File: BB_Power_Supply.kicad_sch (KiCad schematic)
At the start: 17 parts, among them J1 Barrel_Jack_Switch, J2 Conn_01x03_Male, J3 Conn_01x02_Male, J4 Screw_Terminal_01x02, J5 Conn_01x03_Male, J6 Conn_01x02_Male, J7 Screw_Terminal_01x02, U1 LM317_TO-220, U2 LM7805_TO220

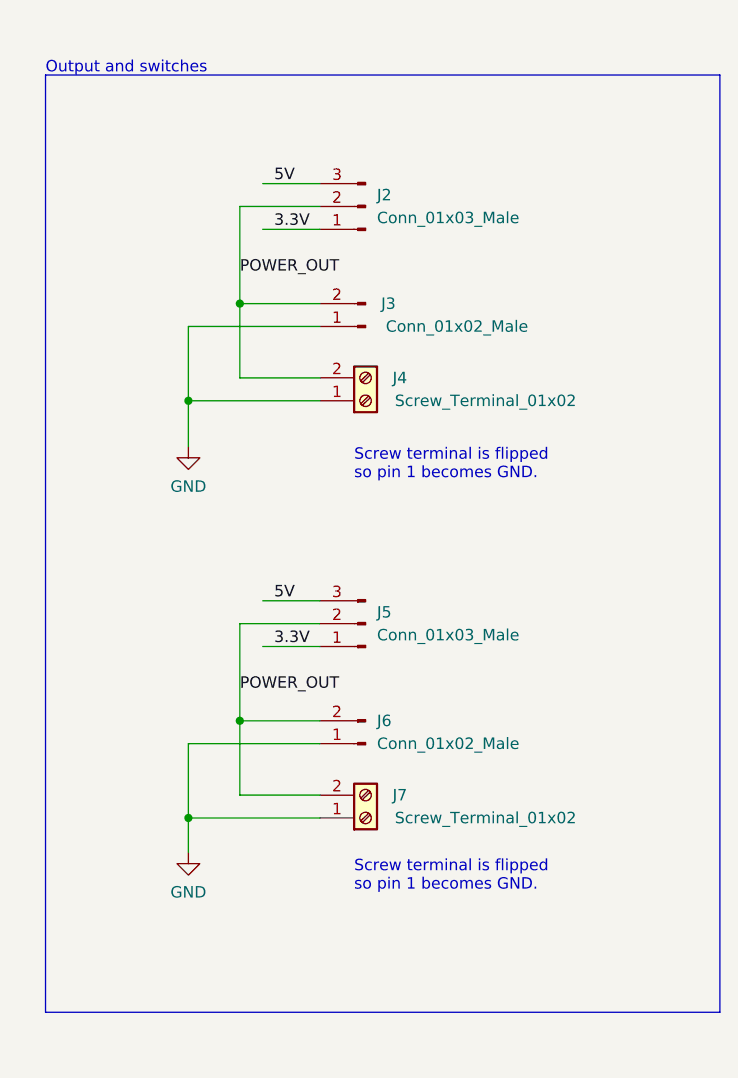
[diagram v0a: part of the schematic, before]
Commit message: Fix issue with POWER_OUT net
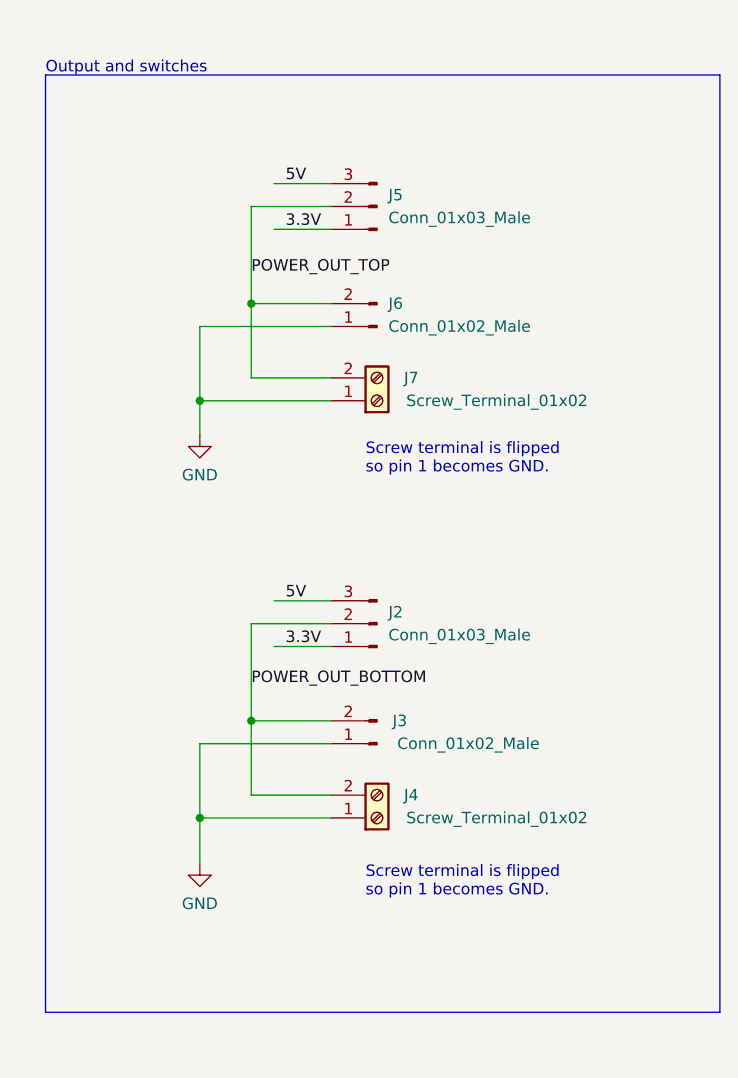
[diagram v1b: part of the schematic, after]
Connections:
- net POWER_OUT renamed POWER_OUT_BOTTOM
- net POWER_OUT_BOTTOM: no longer J5.2 (Pin_2), J6.2 (Pin_2), J7.2 (Pin_2)
- new net POWER_OUT_TOP: J5.2 (Pin_2), J6.2 (Pin_2), J7.2 (Pin_2)
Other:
- moved on the sheet: J2, J3, J4, J5, J6, J7
